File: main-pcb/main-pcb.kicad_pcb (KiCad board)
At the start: 10 copper layers, 130 x 90 mm, 444 parts, among them J1 CONN_01X03, J10 CONN_DUMPTRUCK_HOST, J11 CONN_01X03, J12 PMOD_HOST, J13 PMOD_HOST, J14 USB_C_Receptacle_USB2.0, J2 CORTEX_DEBUG_ETM, J3 XILINX_JTAG, J4 CORTEX_DEBUG_ETM, J5 CONN_01X03, J6 0826-1G1T-23-F, J7 CONN_DUMPTRUCK_HOST, J8 CONN_DUMPTRUCK_HOST, J9 CONN_DUMPTRUCK_HOST, M1 MECHANICAL, M2 SCREWHOLE, M3 SCREWHOLE, M4 SCREWHOLE, M5 SCREWHOLE, M6 MECHANICAL, M7 MECHANICAL, M8 MECHANICAL, M9 MECHANICAL, Q1 SSM6N58NU, SW1 SWITCH, SW2 SWITCH, U1 XC7S100-1FGGA484C, U10 NCP45525IMNTWG-H, U11 LTC3374-QFN, U12 AT24MAC402, U13 ECS-1612MV-250-CN, U14 STM32H735-UFBGA176-25, U15 S27KL0642GABHB020, U16 ECS-1612MV-250-CN, U17 S27KS0642GABHI030, U18 ECS-1612MV-250-CN, U19 INA230, U2 STM32L431-QFN48, U20 KSZ9031RN, U21 RCLAMP0514M, U22 RCLAMP0514M, U23 NCP45525IMNTWG-H, U24 IS25WP256D-JLLE, U25 INA230, U26 74LVC1T45, U27 NCP45525IMNTWG-H, U28 INA230, U29 NCP45525IMNTWG-H, U3 INA230, U30 INA230, U31 NCP45525IMNTWG-H, U32 INA230, U33 19-C47/RSGHBHC-5V01/2T, U34 19-C47/RSGHBHC-5V01/2T, U35 19-C47/RSGHBHC-5V01/2T, U36 19-C47/RSGHBHC-5V01/2T, U37 19-C47/RSGHBHC-5V01/2T, U38 19-C47/RSGHBHC-5V01/2T, U39 NCP45525IMNTWG-H, U4 INA230, U5 INA230, U6 INA230, U7 INA230, U8 INA230, U9 INA230

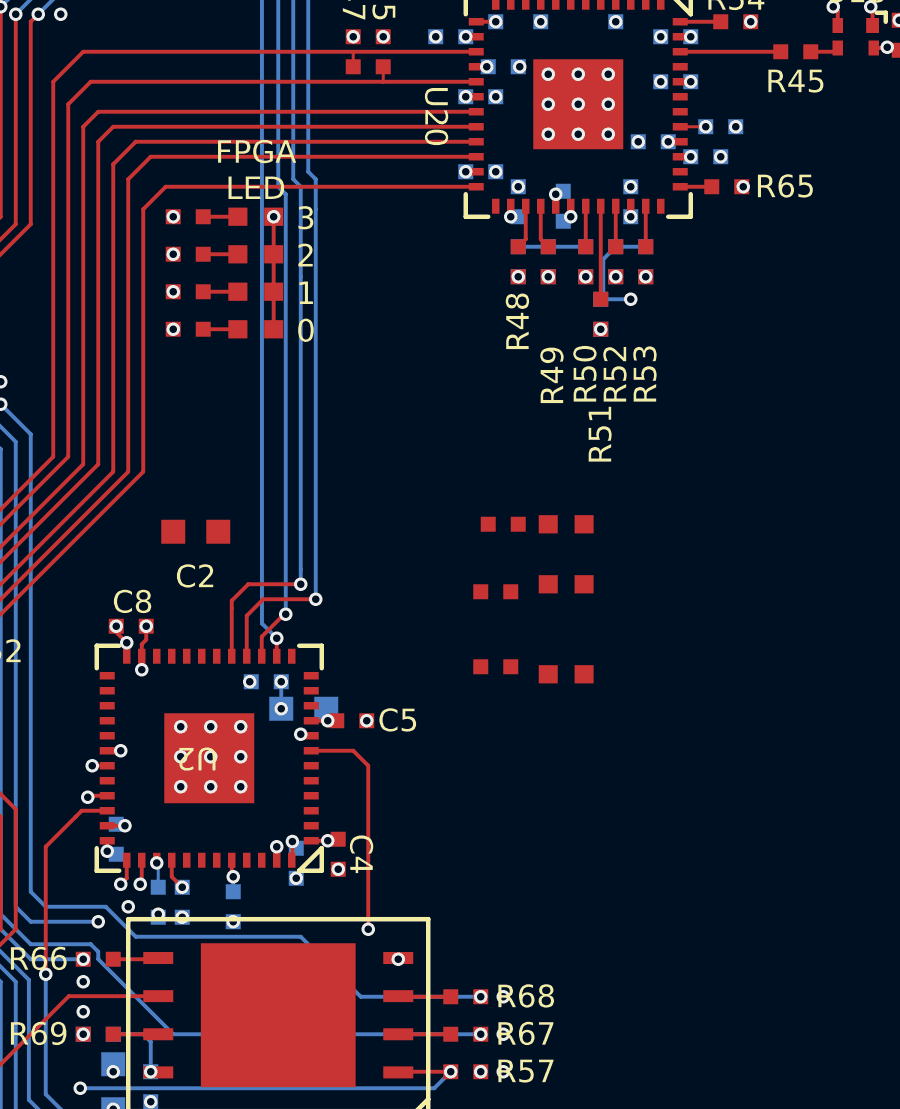
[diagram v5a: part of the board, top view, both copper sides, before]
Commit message: Continued routing RGMII PHY
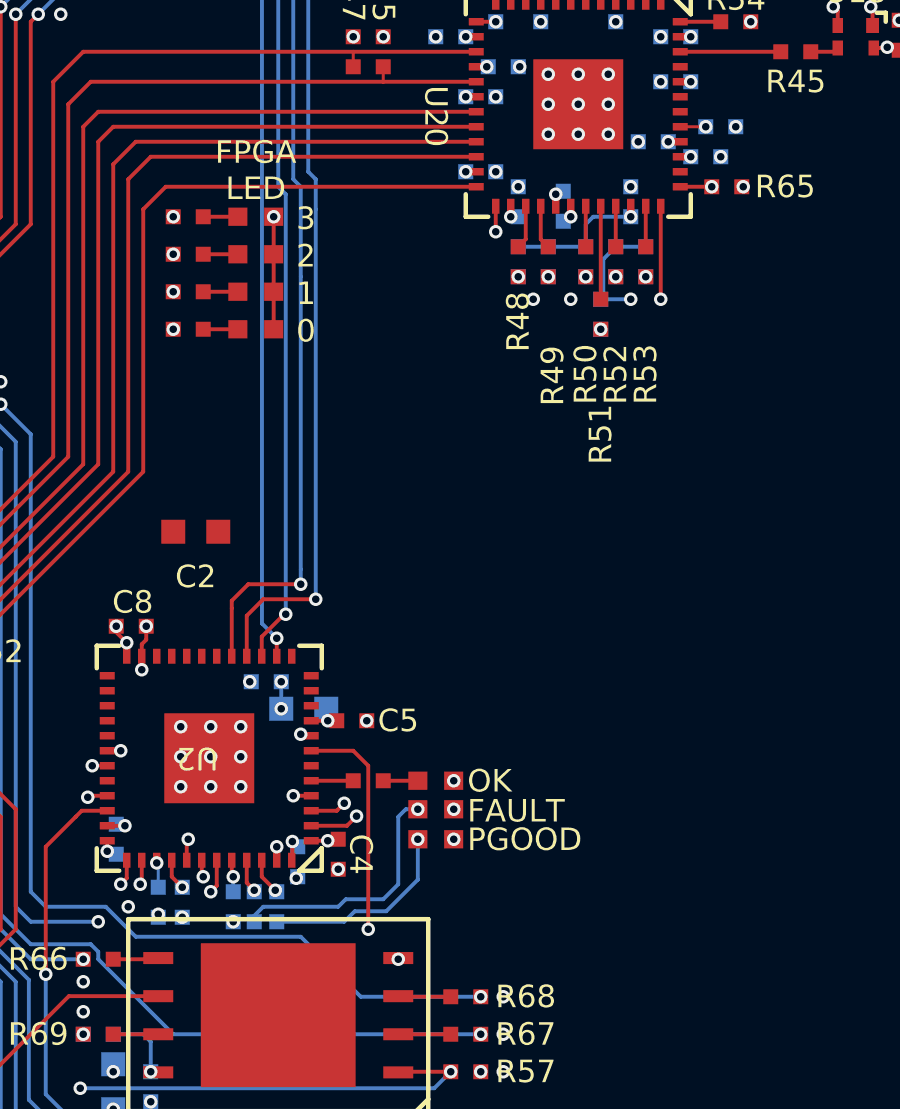
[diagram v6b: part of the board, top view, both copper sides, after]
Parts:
- R2, R4: moved to B.Cu
- moved R2 14.8 mm to (122.0, 98.8), turned to -90 degrees
- moved D1 11.4 mm to (127.2, 96.5), turned to 180 degrees
- moved R4 11.3 mm to (121.2, 98.8), turned to -90 degrees
- moved D2 7.86 mm to (127.2, 94.5), turned to 180 degrees
- moved R3 7.60 mm to (125.0, 94.5)
- moved D3 6.26 mm to (127.2, 95.5), turned to 180 degrees
- moved C6 0.07 mm to (122.7, 97.2)
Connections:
- C201 pad 1: Net-(U33-DIN) -> Net-(U37-DIN)
- R108 pad 2: Net-(U33-DIN) -> Net-(U37-DIN)
- R109 pad 2: Net-(U33-DIN) -> Net-(U37-DIN)
- R59 pad 1: /3V3 -> /1V8
- R60 pad 1: /3V3 -> /1V8
- R61 pad 1: /3V3 -> /1V8
- U1 pad N19: /Ethernet/ETH_RX_DV -> /Ethernet/RGMII_TX_EN
- U1 pad N20: /Ethernet/ETH_RXD1 -> /Ethernet/ETH_RXD3
- U1 pad P20: /Ethernet/ETH_RXD0 -> /Ethernet/ETH_RXD2
- U1 pad P21: /Ethernet/ETH_RXD3 -> /Ethernet/ETH_LED2_N_1V8_INV
- U1 pad P22: /Ethernet/ETH_RXD2 -> /Ethernet/ETH_LED1_N_1V8_INV
- U1 pad R18: /Ethernet/ETH_MDC -> /Ethernet/ETH_RXD1
- U1 pad R19: /Ethernet/ETH_LED1_N_1V8_INV -> /Ethernet/ETH_RXD0
- U1 pad T19: /Ethernet/ETH_RST_N -> /Ethernet/ETH_RX_DV
- U1 pad T20: /Ethernet/ETH_LED2_N_1V8_INV -> /Ethernet/ETH_MDC
- U1 pad U20: /Ethernet/RGMII_TX_EN -> /Ethernet/ETH_RST_N
- U2 pad 20: /Power supply/SUPER_PWRGOOD_LED -> /Power supply/1V2_EN
- U2 pad 29: /INA_ALERT -> /Power supply/1V0_EN
- U2 pad 32: /Power supply/SUPER_SYSOK_LED -> /Power supply/3V3_EN
- U2 pad 41: /Power supply/1V0_EN -> /INA_ALERT
- U2 pad 46: /Power supply/2V5_EN -> /Power supply/SUPER_PWRGOOD_LED
- U2 pad 5: /Power supply/3V3_EN -> /Power supply/SUPER_SYSOK_LED
- U2 pad 6: /Power supply/1V2_EN -> /Power supply/2V5_EN
- U36 pad 1: Net-(U36-DOUT) -> unconnected-(U36-DOUT-Pad1)
- U37 pad 3: Net-(U36-DOUT) -> Net-(U37-DIN)
- U38 pad 1: unconnected-(U38-DOUT-Pad1) -> Net-(U33-DIN)
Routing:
- net /Ethernet/ETH_MDIO: track 7.46 -> 44.7 mm, vias 1 -> 2
- net /Ethernet/ETH_MDC: track 6.16 -> 40.6 mm, vias 1 -> 2
- net /Ethernet/ETH_RX_CLK: track 6.46 -> 40.2 mm
- net /Ethernet/ETH_RX_DV: track 5.96 -> 37.6 mm
- net /Ethernet/ETH_RXD1: track 4.50 -> 35.8 mm
- net /Ethernet/ETH_RXD0: track 4.71 -> 35.1 mm
- net /SUPER_I2C_SDA: track 125.0 -> 153.9 mm, vias 5 -> 6
- net /Ethernet/RGMII_TX_EN: track 5.21 -> 33.4 mm, vias 1 -> 2
- net /Ethernet/ETH_RXD2: track 4.41 -> 32.5 mm
- net /SUPER_I2C_SCL: track 116.5 -> 141.5 mm, vias 5 -> 6
- net /Ethernet/ETH_RXD3: track 7.08 -> 31.0 mm
- net /INA_ALERT: track 114.2 -> 134.7 mm, vias 4 -> 5
- net /GND: track 1716.8 -> 1731.0 mm, vias 547 -> 552
- net /1V8: track 283.8 -> 293.3 mm
- net Net-(D3-A): track 0.00 -> 8.44 mm, vias 0 -> 1
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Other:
- board text added: "FAULT"
- board text added: "OK"
- board text added: "PGOOD"
